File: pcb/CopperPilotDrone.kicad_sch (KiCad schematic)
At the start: 68 parts, among them IC1 TP4056, J1 USB_C_Receptacle_USB2.0, J2 Conn_01x02_Female, J3 B2B-PH-SM4-TB(LF)(SN), J4 Conn_01x02_Female, J5 Conn_01x02_Female, J6 Conn_01x02_Female, SW1 PCM12SMTR, SW2 TS-1187A, SW3 TS-1187A, T1 SI2302DS-T1, T2 SI2302DS-T1, T3 SI2302DS-T1, T4 SI2302DS-T1, U2 AO3401, U3 AP2112K-3.3TRG1, U8 ESP32-S3-WROOM-1-N8R8, U9 MPU-6050

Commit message: feat(dfm): apply LionCircuits Standard Tier DFM upgrades and dual Turnkey/DNP exports
- Upsize all 83 signal vias and 12 U8 pad 41 thermal holes from 0.30/0.60 mm to 0.35/0.65 mm to meet LionCircuits Standard Tier (>= 0.35 mm drill) without surcharges
- Remove F.Paste from U9 (MPU-6050 QFN-24) center pad 25 per TDK InvenSense specification (Rev 3.4 Section 11.2) to prevent reflow solder float
- Synchronize schematic and PCB MPN properties with verified Western distributor (Element14 / Mouser / DigiKey) part numbers across all 28 Tier-1 BOM lines
- Export F.Paste and B.Paste stencil Gerbers, Safe Turnkey DNP BOM/CPL variants (excluding IC1 and U9 portal placeholders), LIONCIRCUITS_ORDER_SPEC.md, and CopperPilotDrone_LionCircuits_Release.zip
- Register standard KiCad 10 SMD footprint libraries in pcb/fp-lib-table and update DEC-003 in review/DECISIONS.md

Co-Authored-By: CopperPilot <noreply@copperpilot.ai>
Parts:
- C10, C11: MPN CL10B105KO8NNNC -> CC0603KRX7R7BB105
- C12, C6: MPN CL10B104KB8NNNC -> CC0603KRX7R9BB104
- D2, D3, D4, D5: MPN 1N5819WS -> PMEG4010EJ,115
- J1: MPN TYPE-C-31-M-12 -> USB4105-GF-A
- LED1: MPN KT-0603B -> LTST-C190TBKT
- LED2: MPN 19-217/GHC-YR1S2/3T -> KPT-1608CGCK
- LED3: MPN KT-0603YG -> LTST-C190KGKT
- R1: MPN 0603WAF4700T5E -> RC0603FR-07470RL
- R10, R11, R18, R19, R20, R21: MPN 0603WAF1002T5E -> RC0603FR-0710KL
- R12, R13, R14: MPN 0603WAF4701T5E -> RC0603FR-074K7L
- R2, R26, R27, R28: MPN 0603WAF1003T5E -> RC0603FR-07100KL
- R22, R23, R29, R30, R31, R32: MPN 0603WAF220JT5E -> RC0603FR-0722RL
- R24, R25: MPN 0603WAF5101T5E -> RC0603FR-075K1L
- R3, R4: MPN 0603WAF1201T5E -> RC0603FR-071K2L
- Rprog1: MPN 0603WAF3301T5E -> RC0603FR-073K3L
- SW2, SW3: MPN TS-1187A-C-C-B -> PTS526SM15SMTR2LFS
- T1, T2, T3, T4: Manufacturer_Part_Number SI2302DS-T1 -> SI2302CDS-T1-GE3
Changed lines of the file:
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@@
 			)
 		)
-		(property "MPN" "TS-1187A-C-C-B"
+		(property "MPN" "PTS526SM15SMTR2LFS"
 			(at 0 0 0)
 			(show_name no)
@@
 			)
 		)
-		(property "MPN" "CL10B105KO8NNNC"
+		(property "MPN" "CC0603KRX7R7BB105"
 			(at 0 0 0)
 			(show_name no)
@@
 			)
 		)
-		(property "Manufacturer_Part_Number" "SI2302DS-T1"
+		(property "Manufacturer_Part_Number" "SI2302CDS-T1-GE3"
 			(at 180.34 1060.35 0)
 			(hide yes)
@@
 			)
 		)
-		(property "Manufacturer_Part_Number" "SI2302DS-T1"
+		(property "Manufacturer_Part_Number" "SI2302CDS-T1-GE3"
 			(at 90.17 1059.08 0)
 			(hide yes)
@@
 			)
 		)
-		(property "MPN" "0603WAF1002T5E"
+		(property "MPN" "RC0603FR-0710KL"
 			(at 0 0 0)
 			(show_name no)
@@
 			)
 		)
-		(property "MPN" "0603WAF4700T5E"
+		(property "MPN" "RC0603FR-07470RL"
 			(at 0 0 0)
 			(show_name no)
@@
 			)
 		)
-		(property "MPN" "0603WAF220JT5E"
+		(property "MPN" "RC0603FR-0722RL"
 			(at 0 0 0)
 			(show_name no)
@@
 			)
 		)
-		(property "MPN" "0603WAF1003T5E"
+		(property "MPN" "RC0603FR-07100KL"
 			(at 0 0 0)
 			(show_name no)
@@
 			)
 		)
-		(property "Manufacturer_Part_Number" "SI2302DS-T1"
+		(property "Manufacturer_Part_Number" "SI2302CDS-T1-GE3"
 			(at 135.89 1060.35 0)
 			(hide yes)
@@
 			)
 		)
-		(property "MPN" "0603WAF220JT5E"
+		(property "MPN" "RC0603FR-0722RL"
 			(at 0 0 0)
 			(show_name no)
@@
 			)
 		)
-		(property "MPN" "0603WAF1002T5E"
+		(property "MPN" "RC0603FR-0710KL"
 			(at 0 0 0)
 			(show_name no)
@@
 			)
 		)
-		(property "Manufacturer_Part_Number" "SI2302DS-T1"
+		(property "Manufacturer_Part_Number" "SI2302CDS-T1-GE3"
 			(at 223.52 1060.35 0)
 			(hide yes)
@@
 			)
 		)
-		(property "MPN" "TYPE-C-31-M-12"
+		(property "MPN" "USB4105-GF-A"
 			(at 0 0 0)
 			(show_name no)
@@
 			)
 		)
-		(property "MPN" "0603WAF1002T5E"
+		(property "MPN" "RC0603FR-0710KL"
 			(at 0 0 0)
 			(show_name no)
@@
 			)
 		)
-		(property "MPN" "0603WAF5101T5E"
+		(property "MPN" "RC0603FR-075K1L"
 			(at 0 0 0)
 			(show_name no)
@@
 			)
 		)
-		(property "MPN" "TS-1187A-C-C-B"
+		(property "MPN" "PTS526SM15SMTR2LFS"
 			(at 0 0 0)
 			(show_name no)
@@
 			)
 		)
-		(property "MPN" "0603WAF1003T5E"
+		(property "MPN" "RC0603FR-07100KL"
 			(at 0 0 0)
 			(show_name no)
@@
 			)
 		)
-		(property "MPN" "CL10B104KB8NNNC"
+		(property "MPN" "CC0603KRX7R9BB104"
 			(at 0 0 0)
 			(show_name no)
@@
 			)
 		)
-		(property "MPN" "0603WAF1002T5E"
+		(property "MPN" "RC0603FR-0710KL"
 			(at 0 0 0)
 			(show_name no)
@@
 			)
 		)
-		(property "MPN" "1N5819WS"
+		(property "MPN" "PMEG4010EJ,115"
 			(at 0 0 0)
 			(show_name no)
@@
 			)
 		)
-		(property "MPN" "CL10B104KB8NNNC"
+		(property "MPN" "CC0603KRX7R9BB104"
 			(at 0 0 0)
 			(show_name no)
@@
 			)
 		)
-		(property "MPN" "0603WAF3301T5E"
+		(property "MPN" "RC0603FR-073K3L"
 			(at 0 0 0)
 			(show_name no)
@@
 			)
 		)
-		(property "MPN" "1N5819WS"
+		(property "MPN" "PMEG4010EJ,115"
 			(at 0 0 0)
 			(show_name no)
@@
 			)
 		)
-		(property "MPN" "0603WAF1201T5E"
+		(property "MPN" "RC0603FR-071K2L"
 			(at 0 0 0)
 			(show_name no)
@@
 			)
 		)
-		(property "MPN" "0603WAF1201T5E"
+		(property "MPN" "RC0603FR-071K2L"
 			(at 0 0 0)
 			(show_name no)
@@
 			)
 		)
-		(property "MPN" "1N5819WS"
+		(property "MPN" "PMEG4010EJ,115"
 			(at 0 0 0)
 			(show_name no)
@@
 			)
 		)
-		(property "MPN" "KT-0603YG"
+		(property "MPN" "LTST-C190KGKT"
 			(at 0 0 0)
 			(show_name no)
@@
 			)
 		)
-		(property "MPN" "0603WAF1002T5E"
+		(property "MPN" "RC0603FR-0710KL"
 			(at 0 0 0)
 			(show_name no)
@@
 			)
 		)
-		(property "MPN" "0603WAF4701T5E"
+		(property "MPN" "RC0603FR-074K7L"
 			(at 0 0 0)
 			(show_name no)
@@
 			)
 		)
-		(property "MPN" "0603WAF1002T5E"
+		(property "MPN" "RC0603FR-0710KL"
 			(at 0 0 0)
 			(show_name no)
@@
 			)
 		)
-		(property "MPN" "1N5819WS"
+		(property "MPN" "PMEG4010EJ,115"
 			(at 0 0 0)
 			(show_name no)
@@
 			)
 		)
-		(property "MPN" "0603WAF4701T5E"
+		(property "MPN" "RC0603FR-074K7L"
 			(at 0 0 0)
 			(show_name no)
@@
 			)
 		)
-		(property "MPN" "CL10B105KO8NNNC"
+		(property "MPN" "CC0603KRX7R7BB105"
 			(at 0 0 0)
 			(show_name no)
@@
 			)
 		)
-		(property "MPN" "0603WAF4701T5E"
+		(property "MPN" "RC0603FR-074K7L"
 			(at 0 0 0)
 			(show_name no)
@@
 			)
 		)
-		(property "MPN" "KT-0603B"
+		(property "MPN" "LTST-C190TBKT"
 			(at 0 0 0)
 			(show_name no)
@@
 			)
 		)
-		(property "MPN" "0603WAF5101T5E"
+		(property "MPN" "RC0603FR-075K1L"
 			(at 0 0 0)
 			(show_name no)
@@
 			)
 		)
-		(property "MPN" "0603WAF1003T5E"
+		(property "MPN" "RC0603FR-07100KL"
 			(at 0 0 0)
 			(show_name no)
@@
 			)
 		)
-		(property "MPN" "0603WAF1003T5E"
+		(property "MPN" "RC0603FR-07100KL"
 			(at 0 0 0)
 			(show_name no)
@@
 			)
 		)
-		(property "MPN" "19-217/GHC-YR1S2/3T"
+		(property "MPN" "KPT-1608CGCK"
 			(at 0 0 0)
 			(show_name no)
@@
 			)
 		)
-		(property "MPN" "0603WAF220JT5E"
+		(property "MPN" "RC0603FR-0722RL"
 			(at 0 0 0)
 			(show_name no)
@@
 			)
 		)
-		(property "MPN" "0603WAF220JT5E"
+		(property "MPN" "RC0603FR-0722RL"
 			(at 0 0 0)
 			(show_name no)
@@
 			)
 		)
-		(property "MPN" "0603WAF220JT5E"
+		(property "MPN" "RC0603FR-0722RL"
 			(at 0 0 0)
 			(show_name no)
@@
 			)
 		)
-		(property "MPN" "0603WAF220JT5E"
+		(property "MPN" "RC0603FR-0722RL"
 			(at 0 0 0)
 			(show_name no)

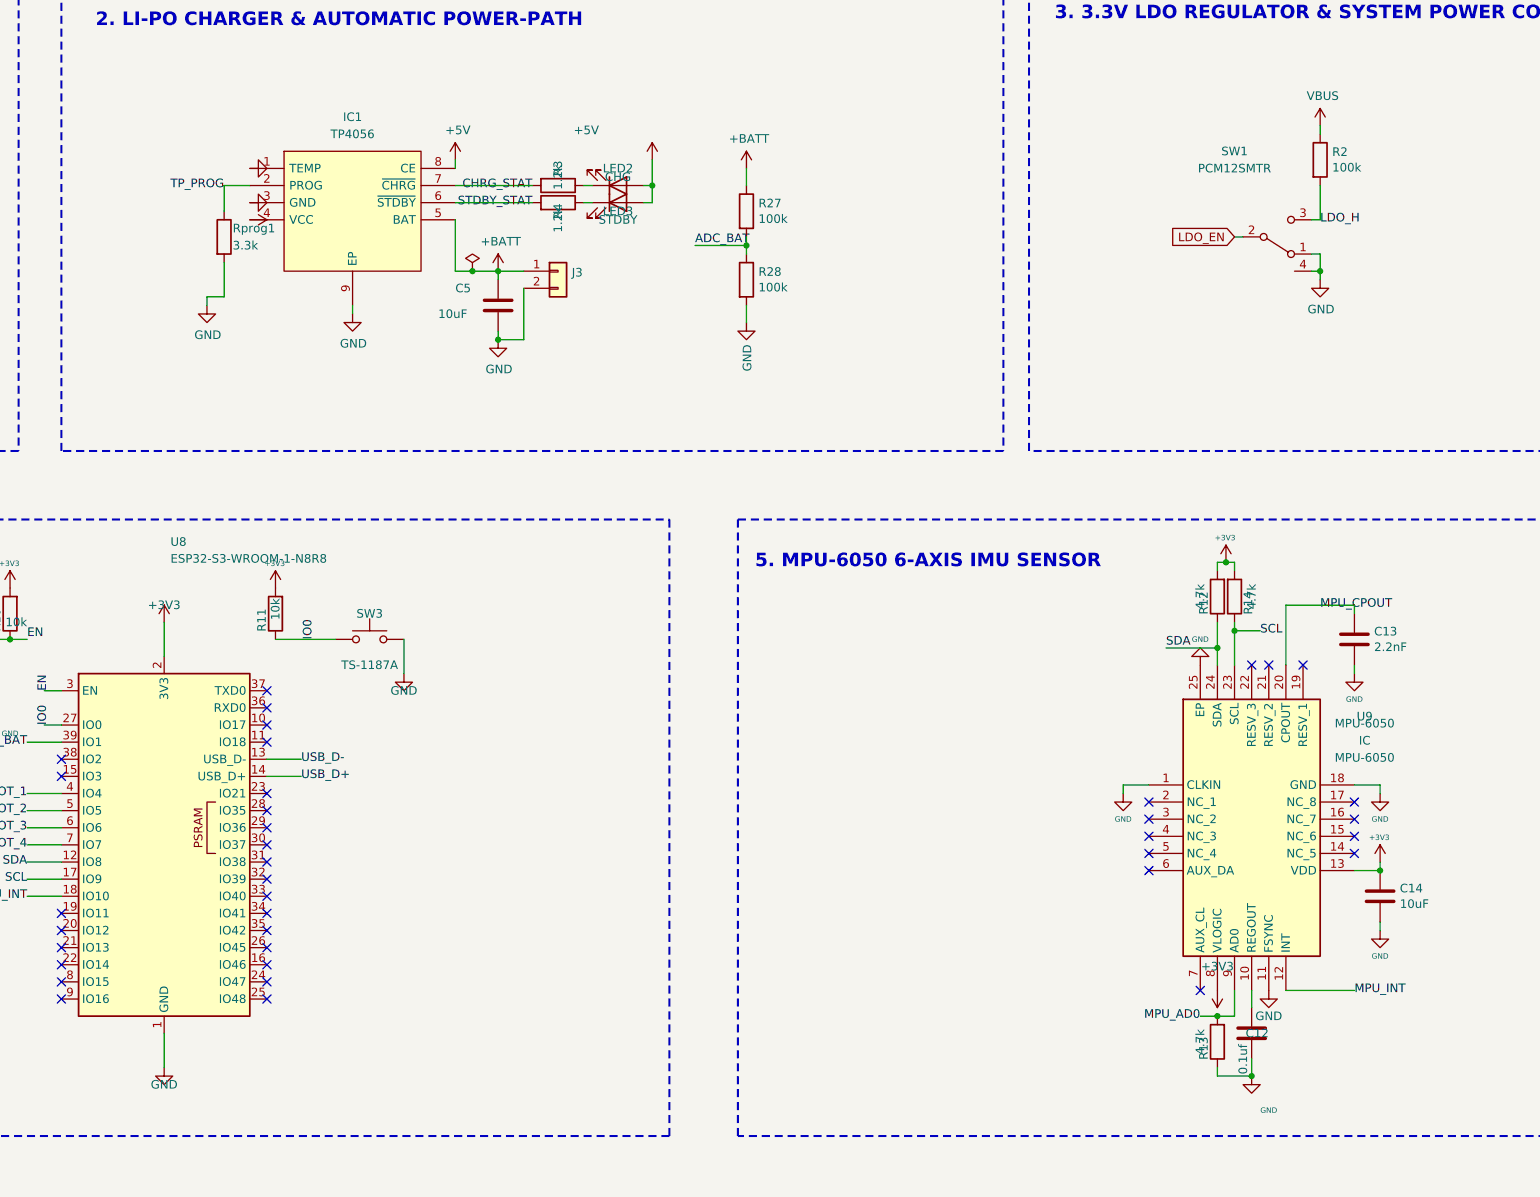
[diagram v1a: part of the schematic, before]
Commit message: feat(sch): redesign IC1 to MCP73833T-AMI/UN and U9 to MPU-6500
- Replace IC1 with Microchip MCP73833T-AMI/UN in MSOP-10 (4.2V 1S LiPo charger with dual STAT1/STAT2 status outputs and 10k THERM grounding resistor R33)
- Replace U9 with native 3.3V TDK InvenSense MPU-6500 in 3x3mm QFN-24 (I2C mode with ~CS pulled high, RESV_GND grounded, and VDDIO/VDD decoupling)
- Register local KiCad symbol and footprint libraries for fully portable builds
- Verify 0 ERC errors or warnings via kicad-cli sch erc

Co-Authored-By: CopperPilot <noreply@copperpilot.ai>
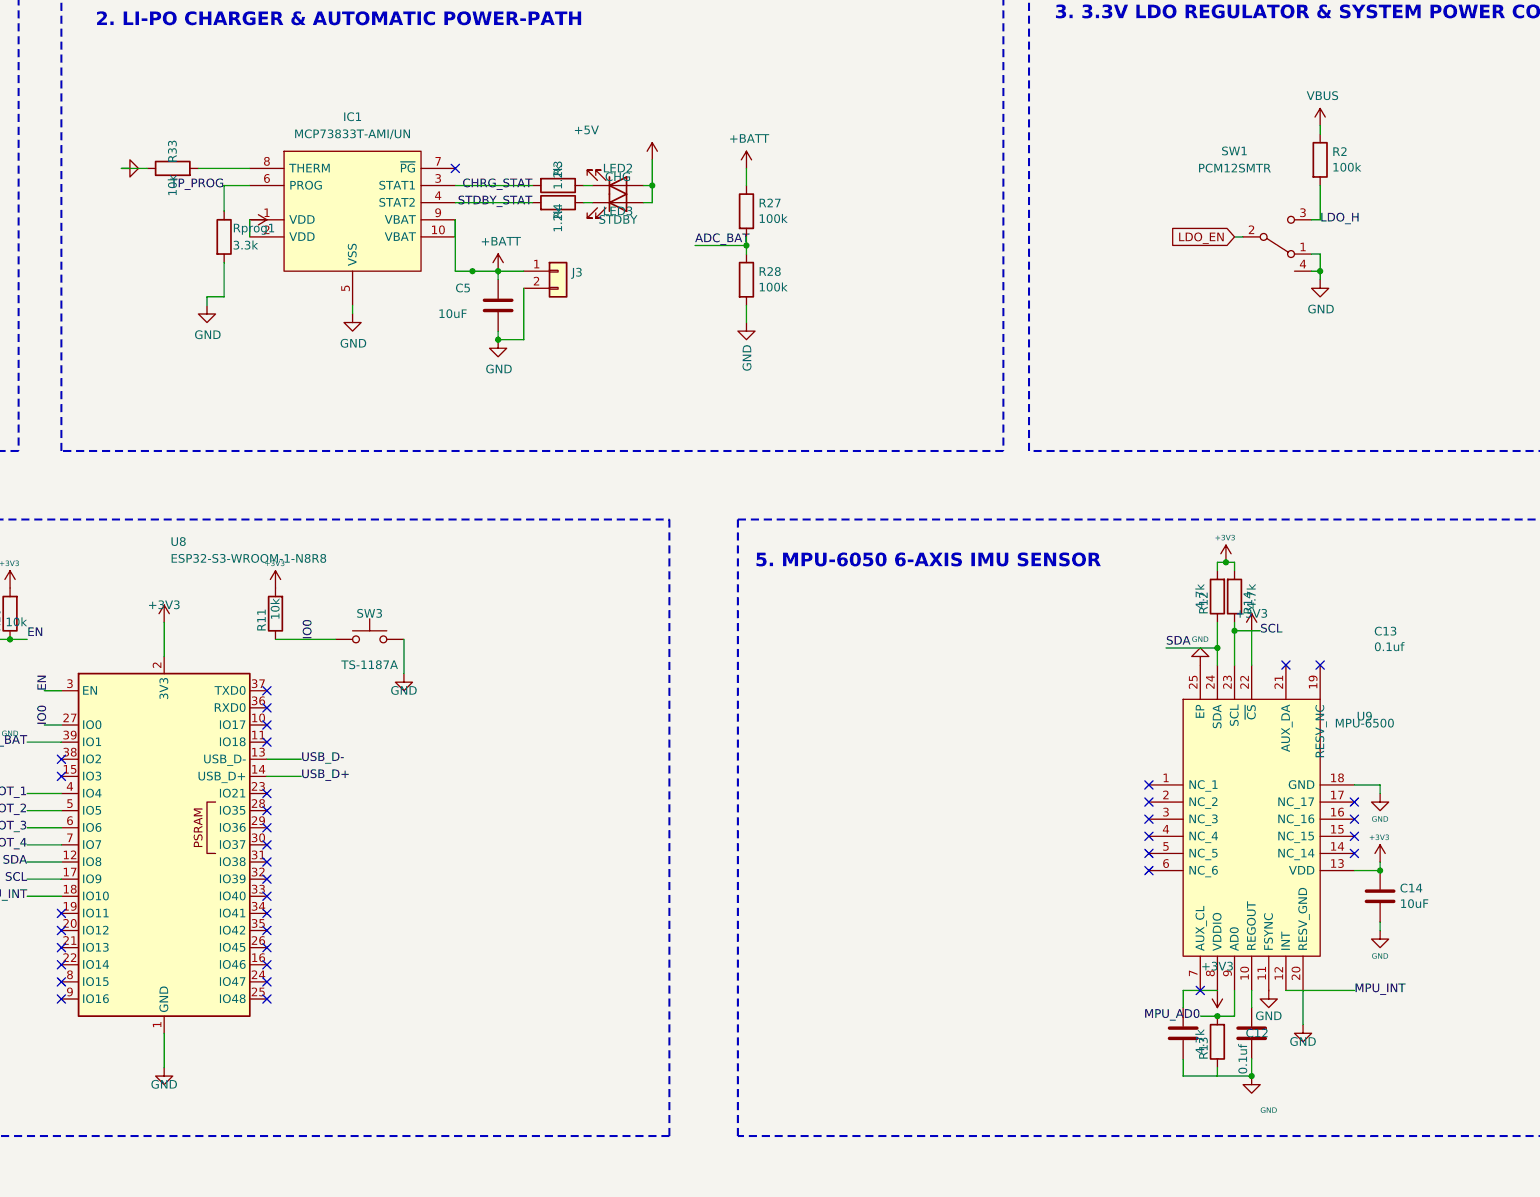
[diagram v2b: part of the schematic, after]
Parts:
- removed IC1: TP4056, tp4056:SOIC127P600X175-9N, symbol TP4056-42-ESOP8:TP4056-42-ESOP8
- removed U9: MPU-6050, MPU6050:MPU6050, symbol MPU-6050:MPU-6050
- added IC1: MCP73833T-AMI/UN, Package_SO:MSOP-10_3x3mm_P0.5mm, symbol MCP73833-AMI-UN:MCP73833-AMI-UN
- added R33: 10k, Resistor_SMD:R_0603_1608Metric, symbol Device:R
- added U9: MPU-6500, Package_DFN_QFN:QFN-24-1EP_3x3mm_P0.4mm_EP1.75x1.6mm, symbol MPU-6500:MPU-6500
- C13: value 2.2nF -> 0.1uf; MPN CC0603KRX7R9BB222 -> CC0603KRX7R9BB104
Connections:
- net MPU_CPOUT is gone; now on net +3V3: C13.1
- net +3V3: now also U9.13 (VDD), U9.22 (~{CS}), U9.8 (VDDIO)
- net +5V: now also IC1.1 (VDD), IC1.2 (VDD)
- net +BATT: now also IC1.10 (VBAT), IC1.9 (VBAT)
- net CHRG_STAT: now also IC1.3 (STAT1)
- net GND: now also IC1.5 (VSS), R33.1, U9.11 (FSYNC), U9.18 (GND), U9.20 (RESV_GND), U9.25 (EP)
- net MPU_AD0: now also U9.9 (AD0)
- net MPU_INT: now also U9.12 (INT)
- net SCL: now also U9.23 (SCL)
- net SDA: now also U9.24 (SDA)
- net STDBY_STAT: now also IC1.4 (STAT2)
- net TP_PROG: now also IC1.6 (PROG)
- net at C12.1: now also U9.10 (REGOUT)
- new net: IC1.8 (THERM), R33.2
- no-connect marks 40 -> 41
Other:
- moved on the sheet: C13
